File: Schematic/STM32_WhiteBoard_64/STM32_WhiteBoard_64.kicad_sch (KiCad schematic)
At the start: 39 parts, among them J1 SWDIO+Serial, J2 USB_B_Micro, J3 Conn_01x22, J4 Conn_01x22, SW1 Boot0, SW2 Reset, U1 STM32F411RET_Arduino, U2 W25Q32JVSSIQ, U4 NCP1117-3.3_SOT223, X1 ASV-8MHz, Y1 ABS25-32.768KHZ-6-T

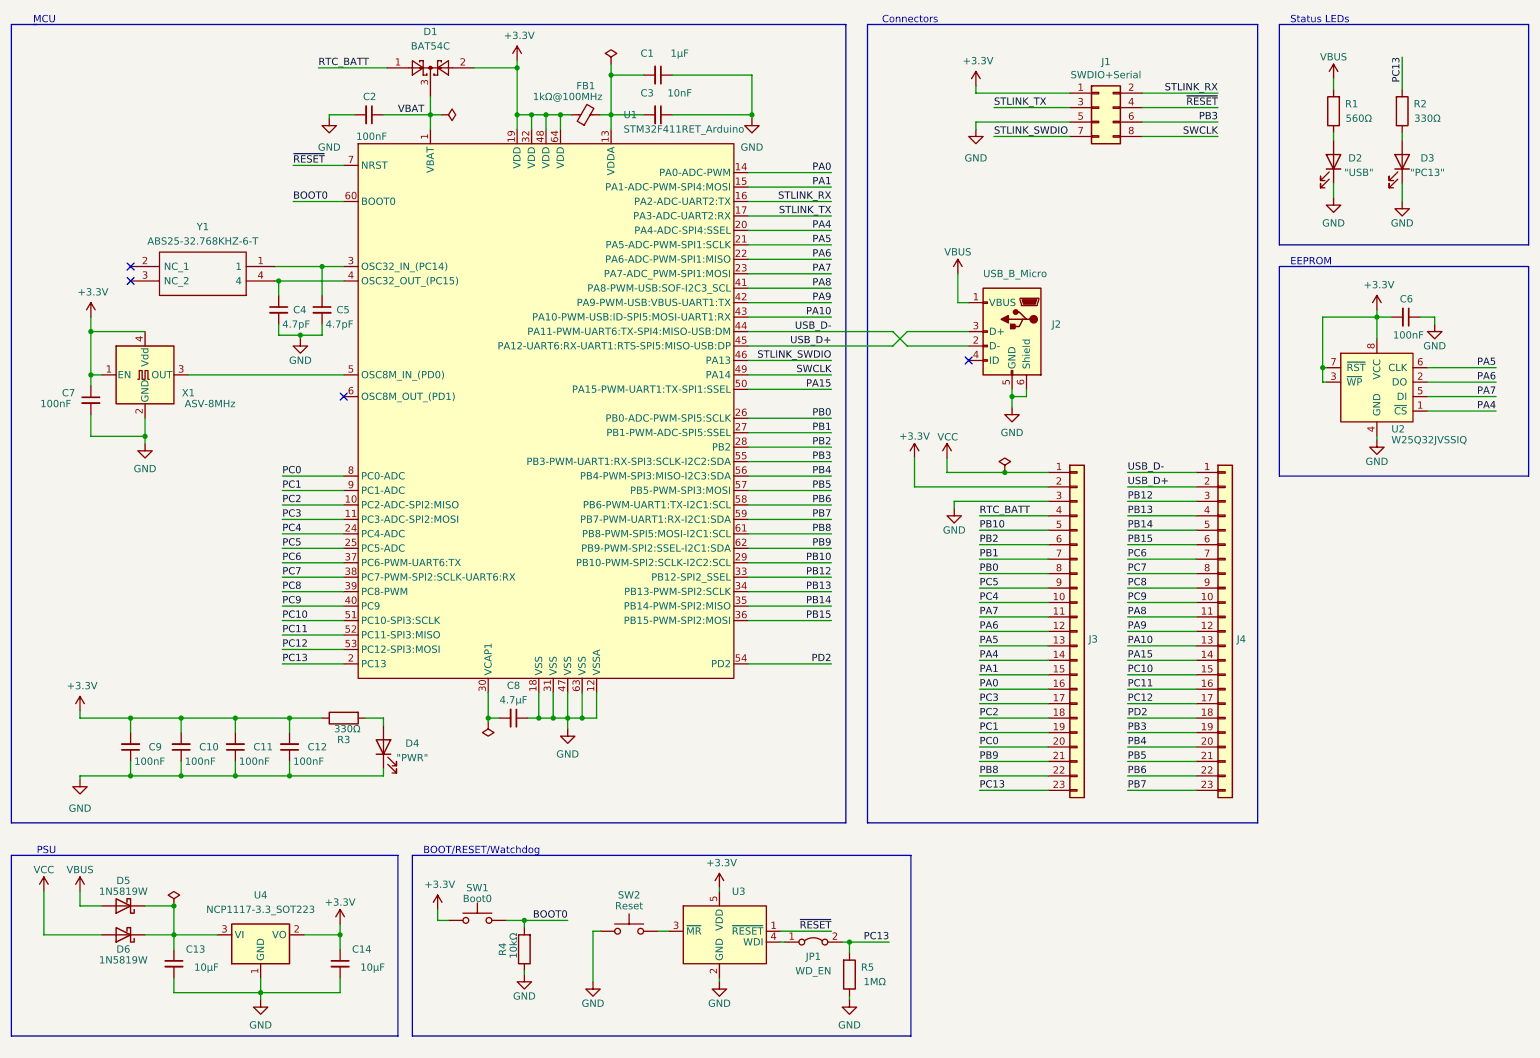
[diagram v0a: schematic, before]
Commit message: Changed footprints for D6, D7
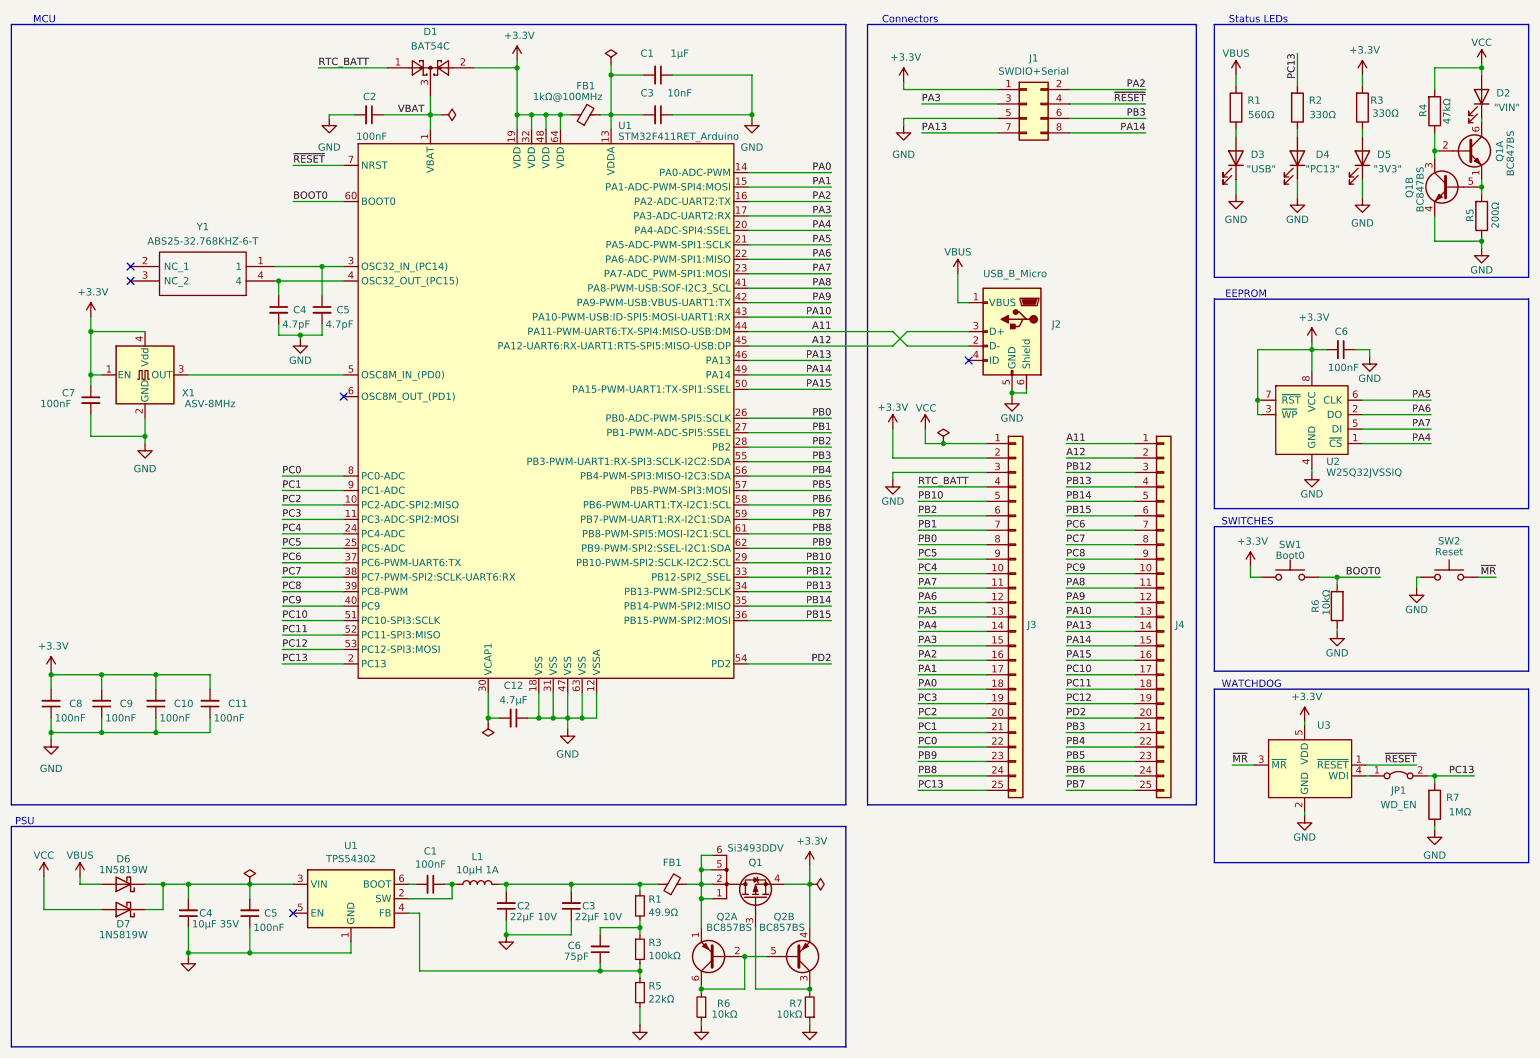
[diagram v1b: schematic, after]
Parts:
- removed C13, C14: 10µF, Capacitor_SMD:C_0603_1608Metric_Pad1.08x0.95mm_HandSolder, symbol Device:C_Small
- removed U4: NCP1117-3.3_SOT223, Package_TO_SOT_SMD:SOT-223-3_TabPin2, symbol Regulator_Linear:NCP1117-3.3_SOT223
- added C1, C5: 100nF, Capacitor_SMD:C_0603_1608Metric_Pad1.08x0.95mm_HandSolder, symbol Device:C_Small
- added C2, C3: 22µF 10V, Capacitor_SMD:C_0603_1608Metric_Pad1.08x0.95mm_HandSolder, symbol Device:C_Small
- added C4: 10µF 35V, Capacitor_SMD:C_0603_1608Metric_Pad1.08x0.95mm_HandSolder, symbol Device:C_Small
- added C6: 75pF, Capacitor_SMD:C_0603_1608Metric_Pad1.08x0.95mm_HandSolder, symbol Device:C_Small
- added D2: "VIN", LED_SMD:LED_0603_1608Metric_Pad1.05x0.95mm_HandSolder, symbol Device:LED
- added FB1: FerriteBead_Small, Inductor_SMD:L_0603_1608Metric_Pad1.05x0.95mm_HandSolder, symbol Device:FerriteBead_Small
- added L1: 10µH 1A, Inductor_SMD:L_Taiyo-Yuden_NR-20xx_HandSoldering, symbol Device:L
- added Q1: Si3493DDV, SamacSys_Parts:SOT95P280X100-6N, symbol myDevices:Si3493DDV
- added Q1: BC847BS, Package_TO_SOT_SMD:SOT-363_SC-70-6, symbol Transistor_BJT:BC847BS
- added Q2: BC857BS, myDevices:SOT-363_SC-70-6-Handsoldering, symbol Transistor_BJT:BC857BS
- added R1: 49.9Ω, Resistor_SMD:R_0603_1608Metric_Pad0.98x0.95mm_HandSolder, symbol Device:R_Small
- added R3: 100kΩ, Resistor_SMD:R_0603_1608Metric_Pad0.98x0.95mm_HandSolder, symbol Device:R_Small
- added R4: 47kΩ, Resistor_SMD:R_0603_1608Metric_Pad0.98x0.95mm_HandSolder, symbol Device:R
- added R5: 200Ω, Resistor_SMD:R_0603_1608Metric_Pad0.98x0.95mm_HandSolder, symbol Device:R
- added R5: 22kΩ, Resistor_SMD:R_0603_1608Metric_Pad0.98x0.95mm_HandSolder, symbol Device:R_Small
- added R6, R7: 10kΩ, Resistor_SMD:R_0603_1608Metric_Pad0.98x0.95mm_HandSolder, symbol Device:R_Small
- added U1: TPS54302, Package_TO_SOT_SMD:SOT-23-6_Handsoldering, symbol Regulator_Switching:TPS54302
- D5: renamed from D4; value "PWR" -> "3V3"
- D6: renamed from D5; footprint Diode_SMD:D_SOD-323_HandSoldering -> Diode_SMD:D_SOD-123
- D7: renamed from D6; footprint Diode_SMD:D_SOD-323_HandSoldering -> Diode_SMD:D_SOD-123
- J3, J4: footprint Connector_PinHeader_2.54mm:PinHeader_1x23_P2.54mm_Vertical -> Connector_PinHeader_2.54mm:PinHeader_1x25_P2.54mm_Vertical; symbol Connector_Generic:Conn_01x23 -> Connector_Generic:Conn_01x25
- renumbered C11 to C10, C12 to C11, C8 to C12, C9 to C8, C10 to C9, D2 to D3, D3 to D4, R4 to R6, R5 to R7
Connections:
- net +3.3V: now also R3.2, Q1.4 (S), Q2.4 (E2); no longer R3.1
- net GND: now also C2.1, C3.1, C4.1, C5.1, Q1.4 (E2), R5.1, R5.2, R6.1, R7.1, U1.1 (GND)
- net PA0: now also J3.18 (Pin_18); no longer J3.16 (Pin_16)
- net PA1: now also J3.17 (Pin_17); no longer J3.15 (Pin_15)
- net PA15: now also J4.16 (Pin_16); no longer J4.14 (Pin_14)
- net PB3: now also J4.21 (Pin_21); no longer J4.19 (Pin_19)
- net PB4: now also J4.22 (Pin_22); no longer J4.20 (Pin_20)
- net PB5: now also J4.23 (Pin_23); no longer J4.21 (Pin_21)
- net PB6: now also J4.24 (Pin_24); no longer J4.22 (Pin_22)
- net PB7: now also J4.25 (Pin_25); no longer J4.23 (Pin_23)
- net PB8: now also J3.24 (Pin_24); no longer J3.22 (Pin_22)
- net PB9: now also J3.23 (Pin_23); no longer J3.21 (Pin_21)
- net PC0: now also J3.22 (Pin_22); no longer J3.20 (Pin_20)
- net PC1: now also J3.21 (Pin_21); no longer J3.19 (Pin_19)
- net PC10: now also J4.17 (Pin_17); no longer J4.15 (Pin_15)
- net PC11: now also J4.18 (Pin_18); no longer J4.16 (Pin_16)
- net PC12: now also J4.19 (Pin_19); no longer J4.17 (Pin_17)
- net PC13: now also J3.25 (Pin_25); no longer J3.23 (Pin_23)
- net PC2: now also J3.20 (Pin_20); no longer J3.18 (Pin_18)
- net PC3: now also J3.19 (Pin_19); no longer J3.17 (Pin_17)
- net PD2: now also J4.20 (Pin_20); no longer J4.18 (Pin_18)
- net VCC: now also D2.2 (A), R4.2
- net ~{MR}: now reaches SW2.2, U3.3 (~{MR})
- net at D5.2 (A): now also R3.1; no longer R3.2
- net at D6.1 (K), D7.1 (K): now also C4.2, C5.2, U1.3 (VIN)
- net STLINK_RX renamed PA2
- net PA2: now also J3.16 (Pin_16)
- net STLINK_SWDIO renamed PA13
- net PA13: now also J4.14 (Pin_14)
- net STLINK_TX renamed PA3
- net PA3: now also J3.15 (Pin_15)
- net SWCLK renamed PA14
- net PA14: now also J4.15 (Pin_15)
- net USB_D+ renamed A12
- net USB_D- renamed A11
- new net: Q1.1 (E1), Q1.5 (B2), R5.2
- new net: C6.1, R3.2, R5.1, U1.4 (FB)
- new net: C6.2, R1.2, R3.1
- new net: C1.1, L1.1, U1.2 (SW)
- new net: C1.2, U1.6 (BOOT)
- new net: C2.2, C3.2, FB1.1, L1.2, R1.1
- new net: FB1.2, Q1.1 (D), Q1.2 (D), Q1.5 (D), Q1.6 (D), Q2.1 (E1)
- new net: Q2.2 (B1), Q2.5 (B2), Q2.6 (C1), R6.2
- new net: Q1.3 (G), Q2.3 (C2), R7.2
- new net: Q1.2 (B1), Q1.3 (C2), R4.1
- new net: D2.1 (K), Q1.6 (C1)
- no-connect marks 4 -> 5
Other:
- note added: "SWITCHES"
- note added: "WATCHDOG"
- note removed: "BOOT/RESET/Watchdog"
- moved on the sheet: C10, C11, C6, C8, C9, D3, D4, D5, D6, D7, J1, JP1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

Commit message: Updated symbols
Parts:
- J3: value Conn_01x22 -> Header1
- J4: value Conn_01x22 -> Header2
- U1: value STM32F411RET_Arduino -> STM32F411RET6; symbol myDevices:STM32F411RET_Arduino -> Retronics_Microcontrollers:STM32F411RET6
- U2: symbol myDevices:W25Q32JVSSIQ -> Retronics_Memory:W25Q32JVSSIQ
- U3: value ~ -> TPS3828-33DBVR; symbol myDevices:TPS3828-33DBVR -> Retronics_Integrated_Circuits:TPS3828-33DBVR
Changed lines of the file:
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@@
       (effects (font (size 1.27 1.27)) (justify left))
     )
-    (property "Value" "Conn_01x22" (at 219.837 123.7996 0)
+    (property "Value" "Header2" (at 219.837 123.7996 0)
       (effects (font (size 1.27 1.27)) (justify left) hide)
     )
@@
       (effects (font (size 1.27 1.27)) (justify left))
     )
-    (property "Value" "Conn_01x22" (at 193.802 123.7996 0)
+    (property "Value" "Header1" (at 193.802 123.7996 0)
       (effects (font (size 1.27 1.27)) (justify left) hide)
     )
@@
     )
   )
-  (symbol (lib_id "myDevices:TPS3828-33DBVR") (at 236.22 147.32 0) (unit 1)
-    (in_bom yes) (on_board yes) (dnp no) (fields_autoplaced)
-    (property "Reference" "U3" (at 244.7641 140.335 0)
-      (effects (font (size 1.27 1.27)) (justify left))
-    )
-    (property "Value" "~" (at 236.22 147.32 0)
-      (effects (font (size 1.27 1.27)))
-    )
-    (property "Footprint" "Package_TO_SOT_SMD:SOT-23-5_HandSoldering" (at 236.22 147.32 0)
+  (symbol (lib_id "Retronics_Integrated_Circuits:TPS3828-33DBVR") (at 236.22 147.32 0) (unit 1)
+    (in_bom yes) (on_board yes) (dnp no)
+    (property "Reference" "U3" (at 245.11 139.065 0)
+      (effects (font (size 1.27 1.27)) (justify left))
+    )
+    (property "Value" "TPS3828-33DBVR" (at 253.365 140.97 0)
+      (effects (font (size 1.27 1.27)))
+    )
+    (property "Footprint" "Package_TO_SOT_SMD:SOT-23-5_HandSoldering" (at 245.11 167.005 0)
       (effects (font (size 1.27 1.27)) hide)
     )
@@
     )
   )
-  (symbol (lib_id "myDevices:STM32F411RET_Arduino") (at 113.03 81.28 0) (unit 1)
+  (symbol (lib_id "Retronics_Microcontrollers:STM32F411RET6") (at 113.03 81.28 0) (unit 1)
     (in_bom yes) (on_board yes) (dnp no)
     (property "Reference" "U1" (at 121.92 34.925 0)
       (effects (font (size 1.27 1.27)) (justify left))
     )
-    (property "Value" "STM32F411RET_Arduino" (at 121.92 36.83 0)
+    (property "Value" "STM32F411RET6" (at 121.92 36.83 0)
       (effects (font (size 1.27 1.27)) (justify left))
     )
@@
     (property "Datasheet" "http://www.st.com/st-web-ui/static/active/en/resource/technical/document/datasheet/DM00115249.pdf" (at 113.03 81.28 0)
       (effects (font (size 1.27 1.27)) hide)
+    )
+    (property "Comments" "" (at 113.03 81.28 0)
+      (effects (font (size 1.27 1.27)))
     )
     (pin "1")
@@
       (effects (font (size 1.27 1.27)) hide)
     )
+    (property "Comments" "" (at 139.065 180.975 0)
+      (effects (font (size 1.27 1.27)))
+    )
     (pin "1")
     (pin "2")
@@
       (effects (font (size 1.27 1.27)) (justify left) hide)
     )
-    (property "Datasheet" "http://uk.rs-online.com/web/p/products/1712795P" (at 83.185 62.23 0)
+    (property "Datasheet" "" (at 83.185 62.23 0)
       (effects (font (size 1.27 1.27)) (justify left) hide)
     )
@@
     (property "Manufacturer_Part_Number" "ABS25-32.768KHZ-6-T" (at 83.185 77.47 0)
       (effects (font (size 1.27 1.27)) (justify left) hide)
+    )
+    (property "Comments" "" (at 61.595 62.23 0)
+      (effects (font (size 1.27 1.27)))
     )
     (pin "1")
@@
     )
   )
-  (symbol (lib_id "myDevices:W25Q32JVSSIQ") (at 245.11 88.265 0) (unit 1)
+  (symbol (lib_id "Retronics_Memory:W25Q32JVSSIQ") (at 245.11 88.265 0) (unit 1)
     (in_bom yes) (on_board yes) (dnp no)
     (property "Reference" "U2" (at 246.38 93.98 0)
@@
     (property "Datasheet" "" (at 250.19 80.645 0)
       (effects (font (size 1.524 1.524)) (justify left) hide)
+    )
+    (property "Comments" "" (at 245.11 88.265 0)
+      (effects (font (size 1.27 1.27)))
     )
     (pin "1")
@@
       (effects (font (size 1.27 1.27)) hide)
     )
+    (property "Comments" "" (at 74.93 170.815 0)
+      (effects (font (size 1.27 1.27)))
+    )
     (pin "1")
     (pin "2")
@@
       (effects (font (size 1.27 1.27)))
     )
-    (property "Value" "1MΩ" (at 269.875 155.575 0)
+    (property "Value" "1MΩ" (at 269.24 155.575 0)
       (effects (font (size 1.27 1.27)))
     )
@@
       (effects (font (size 1.27 1.27)) hide)
     )
-    (property "Datasheet" "http://www.abracon.com/Oscillators/ASV.pdf" (at 36.195 78.74 0)
-      (effects (font (size 1.27 1.27)) hide)
+    (property "Datasheet" "" (at 36.195 78.74 0)
+      (effects (font (size 1.27 1.27)) hide)
+    )
+    (property "Comments" "" (at 38.735 78.74 0)
+      (effects (font (size 1.27 1.27)))
     )
     (pin "1")
@@
       (effects (font (size 1.27 1.27)) hide)
     )
-    (pin "1")
+    (property "Comments" "" (at 153.035 180.975 0)
+      (effects (font (size 1.27 1.27)))
+    )
+    (pin "1")

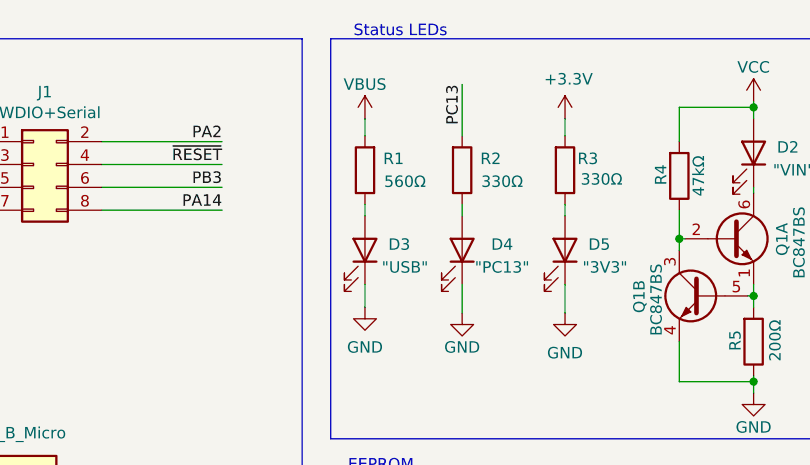
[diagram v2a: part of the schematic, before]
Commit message: Changed component value
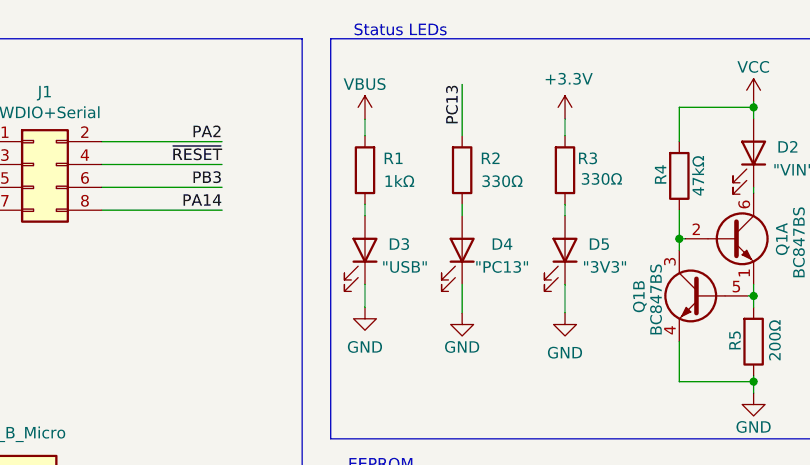
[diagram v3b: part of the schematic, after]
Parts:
- R1: value 560Ω -> 1kΩ
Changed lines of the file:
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@@
       (effects (font (size 1.27 1.27)))
     )
-    (property "Value" "560Ω" (at 234.95 33.02 0)
+    (property "Value" "1kΩ" (at 234.315 33.02 0)
       (effects (font (size 1.27 1.27)))
     )

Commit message: Added pull-up resistor for Reset
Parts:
- added R5: 10kΩ, Resistor_SMD:R_0603_1608Metric_Pad0.98x0.95mm_HandSolder, symbol Device:R
- C1: value 1µF -> 4.7µF
- renumbered R5 to R6, R6 to R7, R7 to R8
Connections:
- net +3.3V: now also R5.2
- net ~{RESET}: now also R5.1

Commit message: Basic IO tests
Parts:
- C1: value 4.7µF -> 10µF
- FB1: value FerriteBead_Small -> 100Ω@100MHz 30mΩ@DC
- Q1: symbol myDevices:Si3493DDV -> Retronics_Discrete:Si3493DDV
- R6: value 200Ω -> 270Ω
- R8: value 1MΩ -> 10kΩ
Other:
- moved on the sheet: FB1, JP1
